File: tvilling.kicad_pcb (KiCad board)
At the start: 2 copper layers, 78.7 x 73.7 mm, 17 parts, among them J1 Conn_01x05_Male, J2 Conn_01x05_Male, J3 Conn_01x05_Male, J4 Conn_01x05_Male, J5 Conn_01x02_Male, SW1 SW_SPDT, SW1 SW_SPST, U1 ESP32-devkit-v1, U2 TB6612_module, U3 TB6612_module

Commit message: Finish v1
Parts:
- removed the D1 at (165.1, 43.8)
- removed the R1 at (179.0, 40.3)
- removed the R2 at (126.4, 92.1)
- removed the SW1 at (126.9, 100.0)
- added J2: Conn_01x02_Male, Connector_PinHeader_2.54mm:PinHeader_1x02_P2.54mm_Vertical, F.Cu at (140.3, 99.1)
- moved SW1 86.8 mm to (131.4, 104.1), turned to -90 degrees
- moved R2 75.7 mm to (114.9, 97.2)
- moved D1 71.2 mm to (132.0, 98.4)
- moved D2 66.8 mm to (134.6, 93.3), turned to 180 degrees
- moved R1 64.5 mm to (122.6, 100.3), turned to 180 degrees
- moved J1 3.81 mm to (146.1, 99.1)
- renumbered D2 to D1, D3 to D2, J5 to J1, J1 to J3, J2 to J4, J3 to J5, J4 to J6, R3 to R1, R4 to R2, U2 to U1, U3 to U2, U1 to U3
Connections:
- D1 pad 2: VCC -> +3.3V
- J1 pad 2: GND -> VCC
- J3 pad 1: +1V1 -> +3.3V
- J4 pad 1: +1V1 -> +3.3V
- J5 pad 1: +1V1 -> +3.3V
- J6 pad 1: +1V1 -> +3.3V
- SW1 pad 1: Net-(R2-Pad2) -> +3.3V
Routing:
- net +3.3V: track 0.00 -> 186.9 mm, vias 0 -> 1
- net +1V1: track 147.1 -> 0.00 mm, vias 1 -> 0
- net /STBY: track 67.2 -> 144.0 mm, vias 0 -> 1
- net VCC: track 191.6 -> 127.5 mm
- net Net-(D2-Pad2): track 0.00 -> 11.1 mm
- net Net-(D1-Pad1): track 0.00 -> 10.2 mm
- net /POS_C: track 101.8 -> 99.7 mm
- net /POS_D: track 91.6 -> 93.2 mm

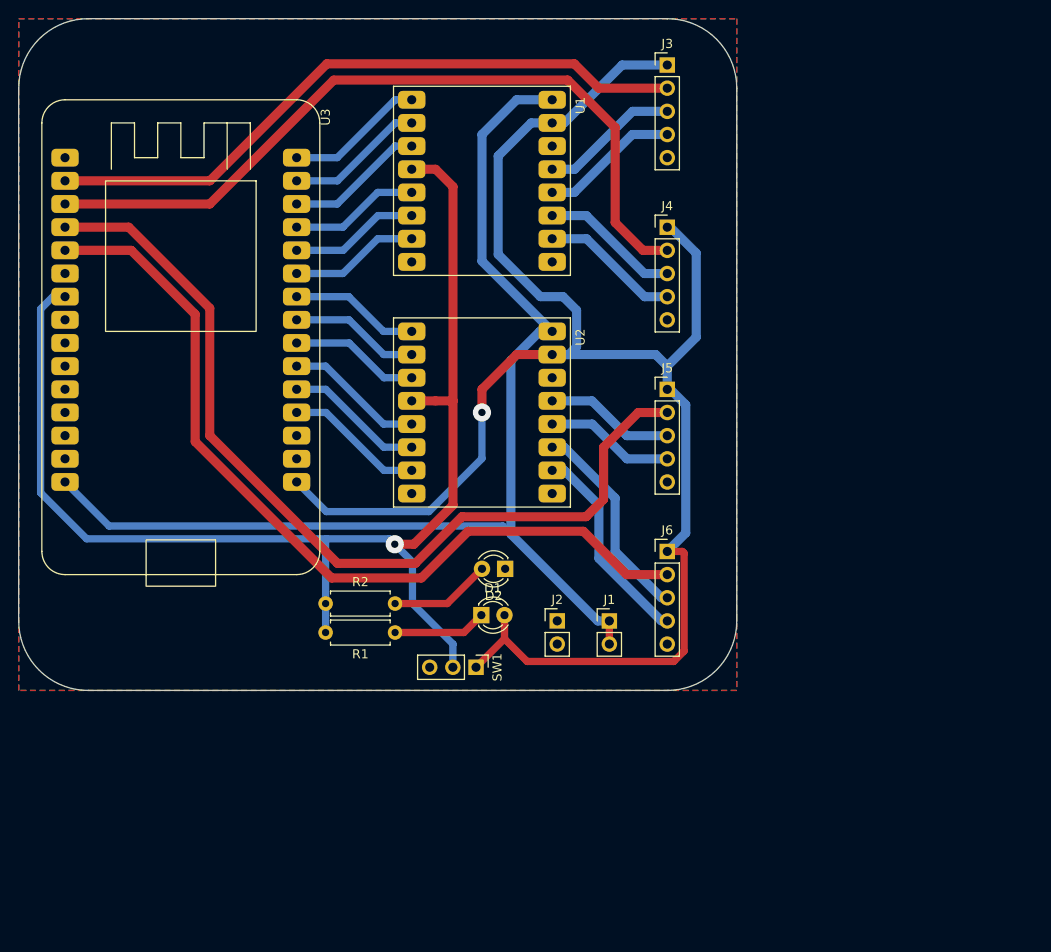
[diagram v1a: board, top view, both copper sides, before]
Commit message: Move traces to bottom copper
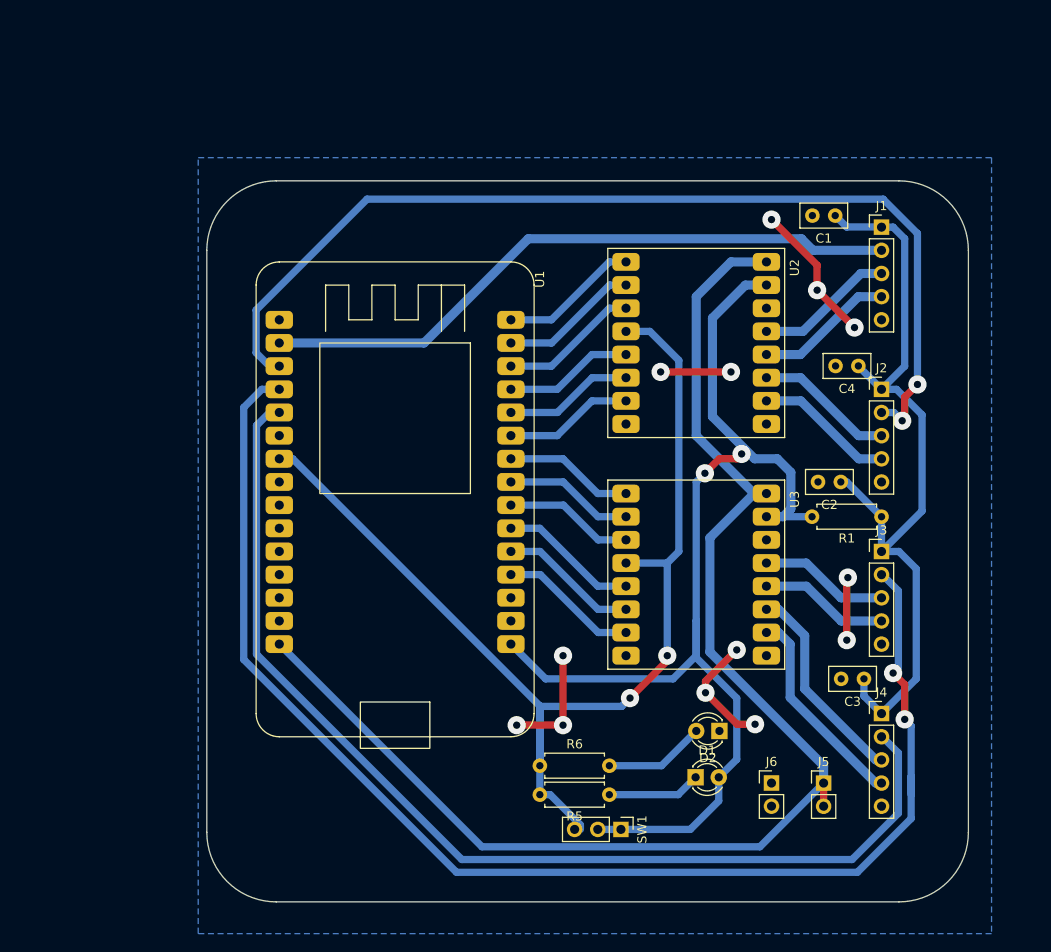
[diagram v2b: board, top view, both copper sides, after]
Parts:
- added C1: 100nF, Capacitor_THT:C_Disc_D5.0mm_W2.5mm_P2.50mm, F.Cu at (170.8, 54.6)
- added C2: 100nF, Capacitor_THT:C_Disc_D5.0mm_W2.5mm_P2.50mm, F.Cu at (171.4, 83.8)
- added C3: 100nF, Capacitor_THT:C_Disc_D5.0mm_W2.5mm_P2.50mm, F.Cu at (174.0, 105.4)
- added C4: 100nF, Capacitor_THT:C_Disc_D5.0mm_W2.5mm_P2.50mm, F.Cu at (173.4, 71.1)
- added R1: 470R, Resistor_THT:R_Axial_DIN0207_L6.3mm_D2.5mm_P7.62mm_Horizontal, F.Cu at (175.9, 87.6)
- D1: value LED -> GREEN
- D2: value LED -> RED
- J1: renamed from J3; value Conn_01x05_Male -> Motor_A
- J2: renamed from J4; value Conn_01x05_Male -> Motor_B
- J3: renamed from J5; value Conn_01x05_Male -> Motor_C
- J4: renamed from J6; value Conn_01x05_Male -> Motor_D
- J5: renamed from J1; value Conn_01x02_Male -> +
- J6: renamed from J2; value Conn_01x02_Male -> -
- R5: renamed from R1; value R -> 470R
- R6: renamed from R2; value R -> 470R
- SW1: value SW_SPDT -> ON/OFF
- moved J2 29.5 mm to (175.9, 73.7)
- moved D1 29.5 mm to (155.5, 116.2)
- moved D2 29.5 mm to (158.1, 111.1)
- moved J1 29.5 mm to (175.9, 55.9)
- moved J4 29.5 mm to (175.9, 109.2)
- moved R5 29.5 mm to (146.1, 118.1)
- moved R6 29.5 mm to (138.4, 114.9)
- moved J3 29.5 mm to (175.9, 91.4)
- moved J6 29.5 mm to (163.8, 116.8)
- moved U1 29.5 mm to (122.6, 83.8)
- moved J5 29.5 mm to (169.5, 116.8)
- moved U2 29.5 mm to (155.6, 68.6)
- moved U3 29.5 mm to (155.6, 94.0)
- moved SW1 23.8 mm to (147.3, 121.9)
- renumbered U3 to U1, U1 to U2, U2 to U3
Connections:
- J1 pad 1: +3.3V -> +3.3VA
- J2 pad 1: +3.3V -> +3.3VA
- J3 pad 1: +3.3V -> +3.3VA
- J4 pad 1: +3.3V -> +3.3VA
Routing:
- net +3.3VA: track 0.00 -> 89.1 mm
- net +3.3V: track 186.9 -> 126.0 mm, vias 1 -> 2
- net GND: track 0.00 -> 55.9 mm, vias 0 -> 13
- net /POS_C: track 99.7 -> 148.3 mm, vias 0 -> 2
- net /POS_D: track 93.2 -> 119.2 mm
- net /POS_B: track 85.5 -> 110.8 mm, vias 0 -> 2
- net VCC: track 127.5 -> 148.1 mm
- net /STBY: track 144.0 -> 123.4 mm, vias 1 -> 2
- net /POS_A: track 72.5 -> 71.3 mm
- removed copper zone on F.Cu, net GND
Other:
- board size 78.7 x 73.7 mm -> 83.5 x 79.1 mm
